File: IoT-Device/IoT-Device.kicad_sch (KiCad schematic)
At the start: 45 parts, among them J1 USB_C_Receptacle_USB2.0_16P, J2 Conn_ARM_JTAG_SWD_10, SW1 B1, SW2 B2, SW3 BOOT_MODE, SW4 RESET, U1 STM32U585VITx, U2 ESP32-C3-WROOM-02, U3 BD33GA5WEFJ

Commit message: add schematics, update metro shield
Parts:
- J1: value USB_C_Receptacle_USB2.0_16P -> USB-C
- J2: value Conn_ARM_JTAG_SWD_10 -> SWD
- U1: value STM32U585VITx -> STM32U585VI
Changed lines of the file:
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@@
 		(dnp no)
 		(property "Reference" "U1"
-			(at 196.088 144.526 0)
-			(effects
-				(font
-					(size 1.27 1.27)
-				)
-			)
-		)
-		(property "Value" "STM32U585VITx"
-			(at 198.628 145.542 0)
+			(at 196.088 154.178 0)
+			(effects
+				(font
+					(size 1.27 1.27)
+				)
+			)
+		)
+		(property "Value" "STM32U585VI"
+			(at 196.088 145.288 0)
 			(effects
 				(font
@@
 			)
 		)
-		(property "Value" "Conn_ARM_JTAG_SWD_10"
+		(property "Value" "SWD"
 			(at 247.65 144.7799 0)
 			(effects
@@
 			)
 		)
-		(property "Value" "USB_C_Receptacle_USB2.0_16P"
+		(property "Value" "USB-C"
 			(at 34.29 24.13 0)
 			(effects

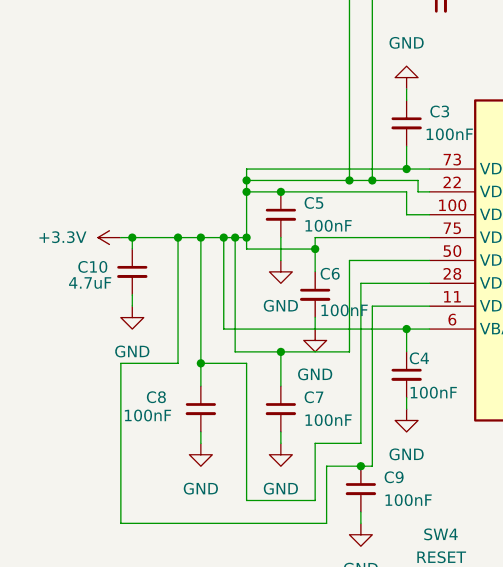
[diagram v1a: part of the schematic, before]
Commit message: update IoT-device schematic, update pcb to free space around more pins
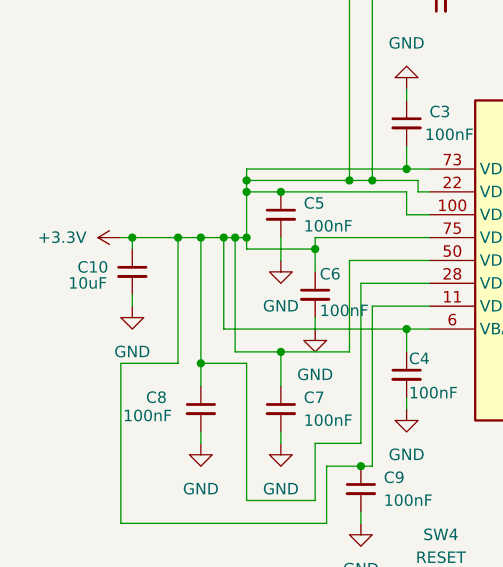
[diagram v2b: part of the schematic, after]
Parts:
- C10: value 4.7uF -> 10uF
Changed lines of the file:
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@@
 			)
 		)
-		(property "Value" "4.7uF"
+		(property "Value" "10uF"
 			(at 17.018 139.7 0)
 			(effects

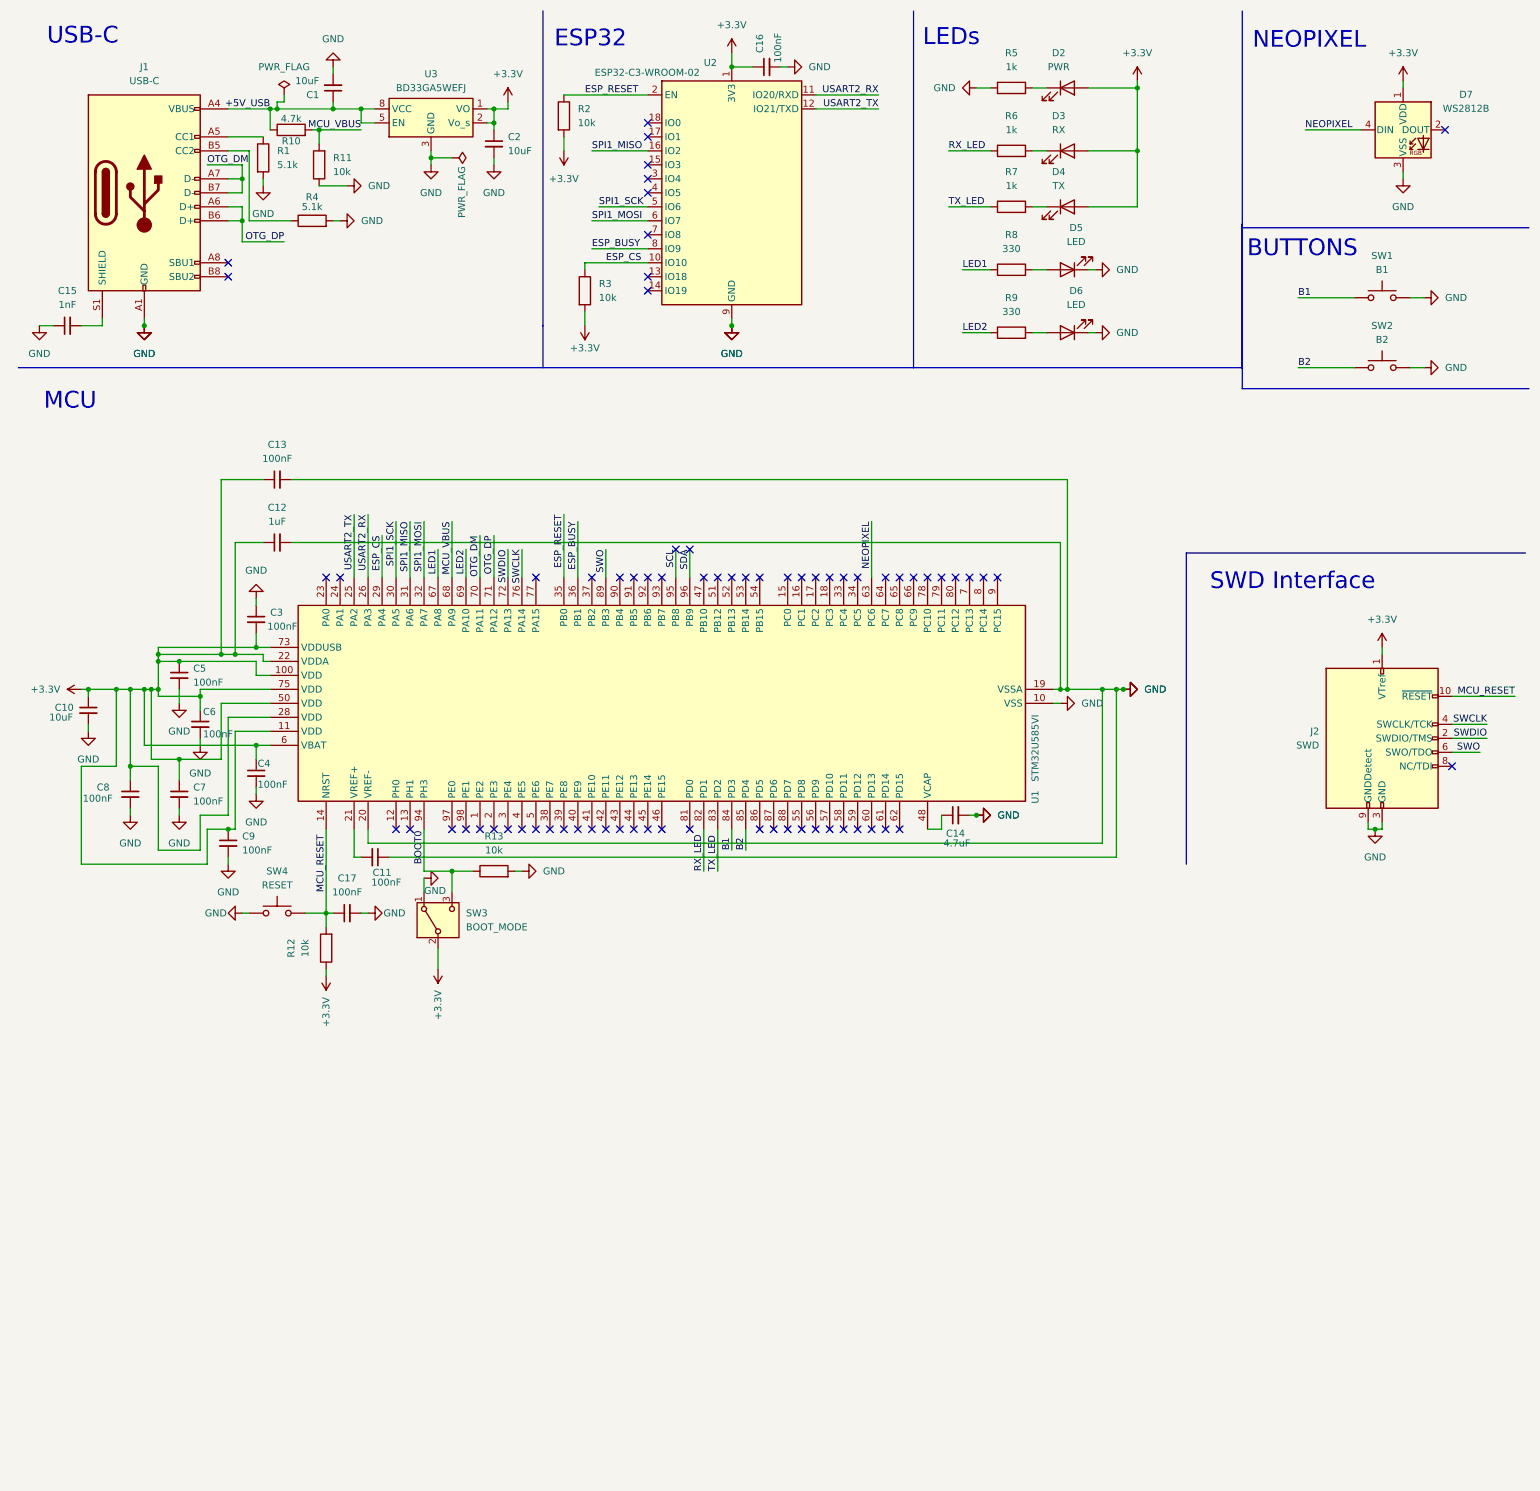
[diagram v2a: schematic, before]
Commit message: add battery power to design
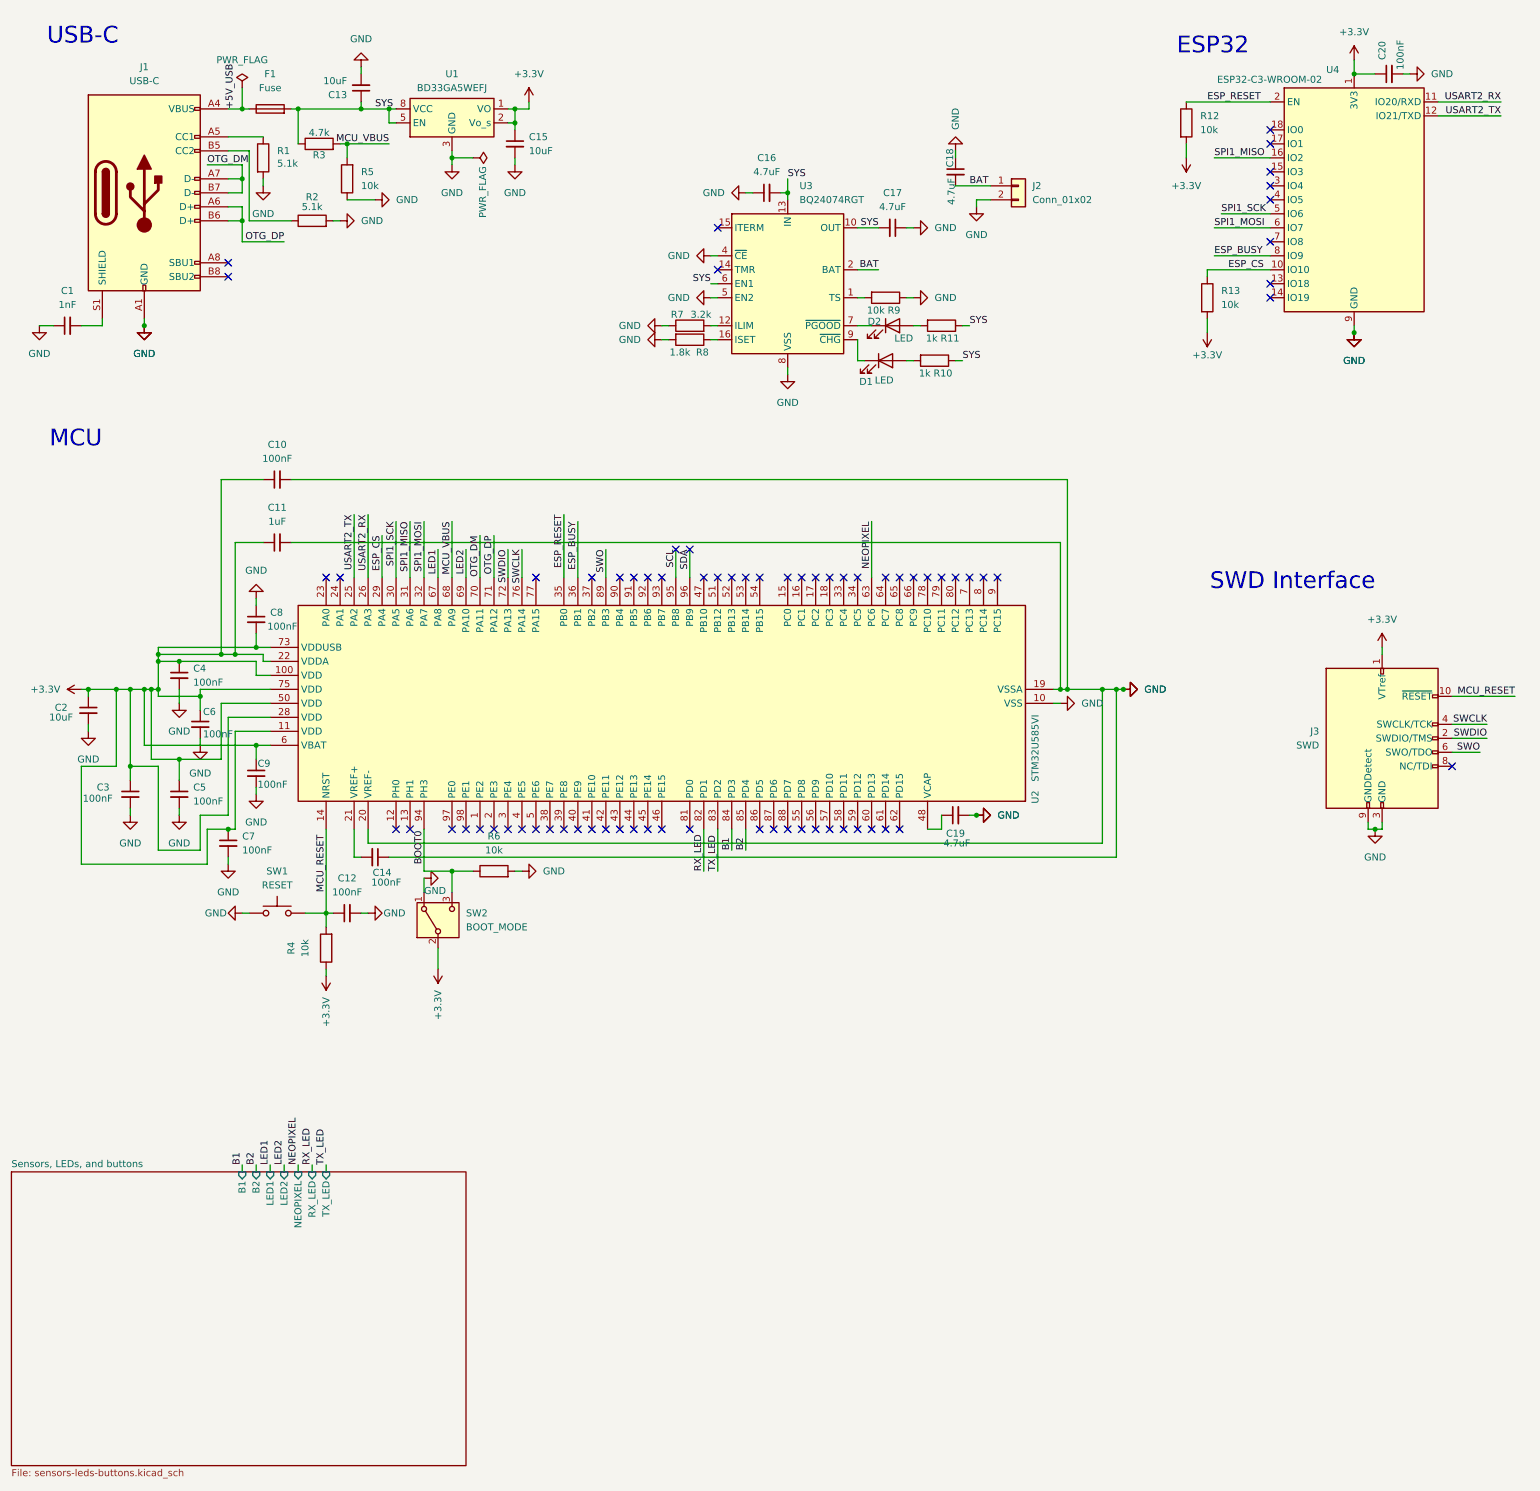
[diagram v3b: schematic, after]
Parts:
- removed D3: RX, LED_SMD:LED_0603_1608Metric, symbol Device:LED
- removed D4: TX, LED_SMD:LED_0603_1608Metric, symbol Device:LED
- removed D5, D6: LED, LED_SMD:LED_0603_1608Metric, symbol Device:LED
- removed D7: WS2812B, LED_SMD:LED_WS2812B_PLCC4_5.0x5.0mm_P3.2mm, symbol LED:WS2812B
- removed R5, R6: 1k, Resistor_SMD:R_0603_1608Metric, symbol Device:R
- removed SW1: B1, Button_Switch_SMD:SW_SPST_PTS647_Sx50, symbol Switch:SW_Push
- removed SW2: B2, Button_Switch_SMD:SW_SPST_PTS647_Sx50, symbol Switch:SW_Push
- added C16, C17, C18: 4.7uF, Capacitor_SMD:C_0603_1608Metric, symbol Device:C_Small
- added D1: LED, LED_SMD:LED_0603_1608Metric, symbol Device:LED
- added F1: Fuse, Fuse:Fuse_0603_1608Metric, symbol Device:Fuse
- added J2: Conn_01x02, Connector_JST:JST_PH_B2B-PH-K_1x02_P2.00mm_Vertical, symbol Connector_Generic:Conn_01x02
- added R10, R11: 1k, Resistor_SMD:R_0603_1608Metric, symbol Device:R
- added U3: BQ24074RGT, Package_DFN_QFN:VQFN-16-1EP_3x3mm_P0.5mm_EP1.6x1.6mm, symbol Battery_Management:BQ24074RGT
- D2: value PWR -> LED
- R7: value 1k -> 3.2k
- R8: value 330 -> 1.8k
- R9: value 330 -> 10k
- renumbered C15 to C1, C13 to C10, C12 to C11, C17 to C12, C1 to C13, C11 to C14, C2 to C15, C14 to C19, C10 to C2, C16 to C20, C8 to C3, C5 to C4, C7 to C5, C9 to C7, C3 to C8, C4 to C9, J2 to J3, R2 to R12, R3 to R13, R4 to R2, R10 to R3, R12 to R4, R11 to R5, R13 to R6, SW4 to SW1, SW3 to SW2, U3 to U1, U1 to U2, U2 to U4
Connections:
- net +3.3V: no longer D2.2 (A)
- net +5V_USB: now also F1.1; no longer C13.1, R3.1, U1.5 (EN), U1.8 (VCC)
- net GND: now also R7.1, R8.2, R9.1, C16.1, C17.1, C18.1, J2.2 (Pin_2), U3.17 (VSS), U3.4 (~{CE}), U3.5 (EN2), U3.8 (VSS)
- net LED1: no longer R8.1
- net LED2: no longer R9.1
- net TX_LED: no longer R7.1
- net at R9.2: now also U3.1 (TS)
- net at D2.1 (K): now also U3.7 (~{PGOOD})
- net at R7.2: now also U3.12 (ILIM)
- new net: D2.2 (A), R11.2
- new net: R8.1, U3.16 (ISET)
- new net: D1.1 (K), U3.9 (~{CHG})
- new net: D1.2 (A), R10.2
- new net BAT: C18.2, J2.1 (Pin_1), U3.2 (BAT), U3.3 (BAT)
- new net SYS: C13.1, C16.2, C17.2, F1.2, R10.1, R11.1, R3.1, U1.5 (EN), U1.8 (VCC), U3.10 (OUT), U3.11 (OUT), U3.13 (IN), U3.6 (EN1)
- no-connect marks 72 -> 73
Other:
- added sheet Sensors, LEDs, and buttons (sensors-leds-buttons.kicad_sch)
- note removed: "BUTTONS"
- note removed: "LEDs"
- note removed: "NEOPIXEL"
- moved on the sheet: C13, C15, C20, R12, R13, R3, R5, U1, U4

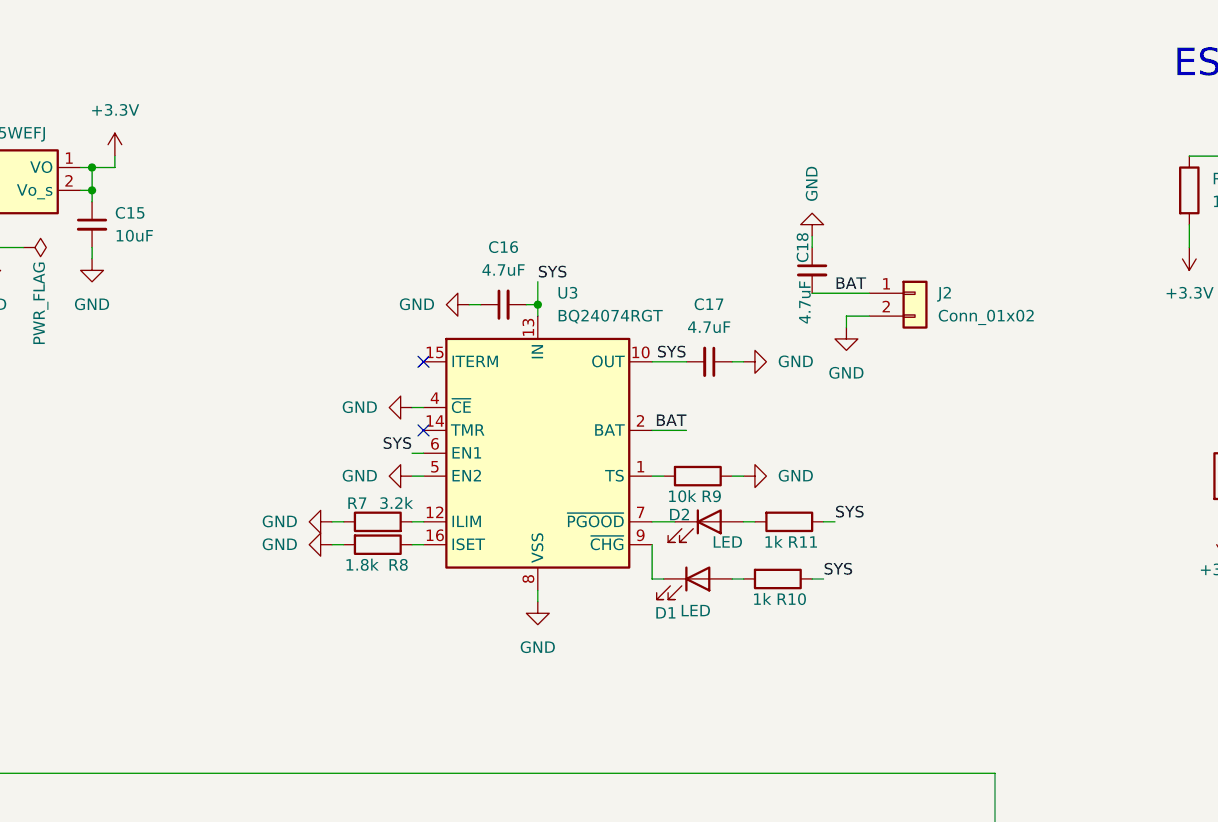
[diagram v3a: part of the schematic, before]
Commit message: add title to battery system section
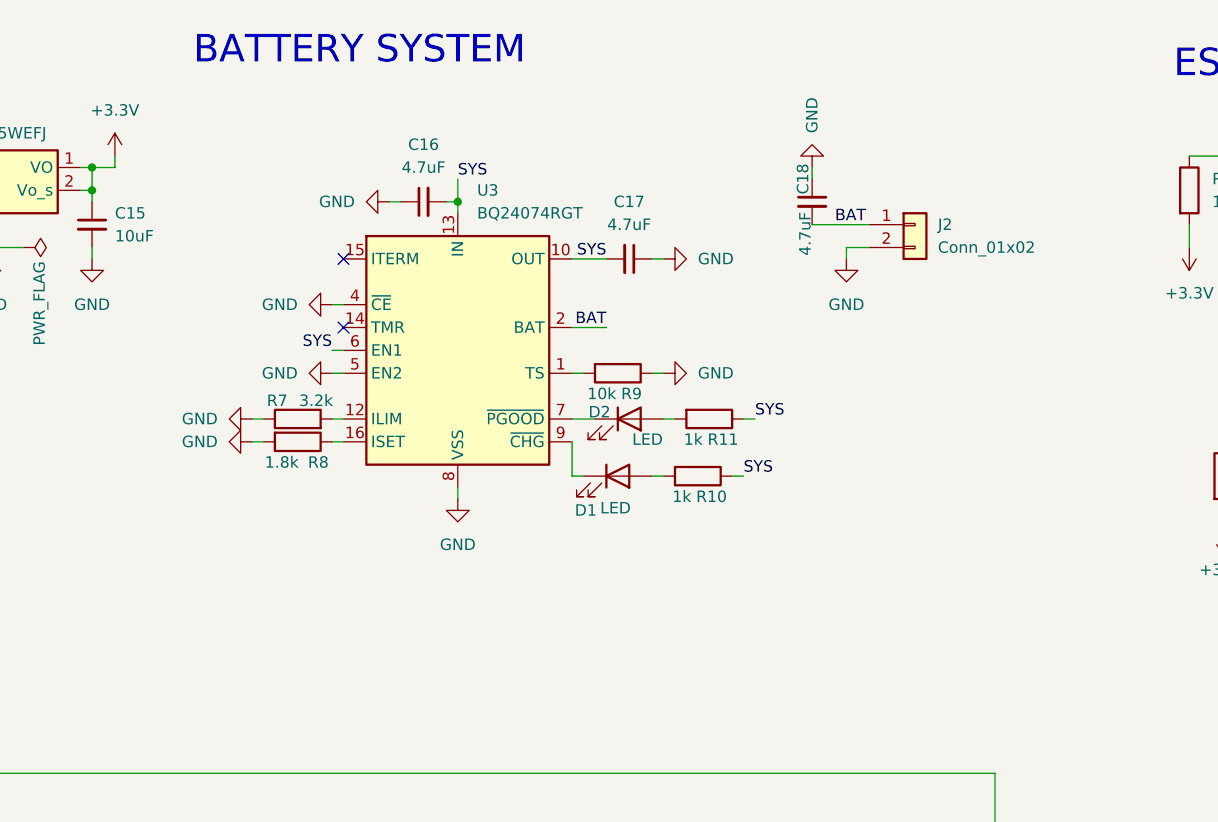
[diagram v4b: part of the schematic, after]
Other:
- note added: "BATTERY SYSTEM"
- moved on the sheet: C16, C17, C18, D1, D2, J2, R10, R11, R7, R8, R9, U3

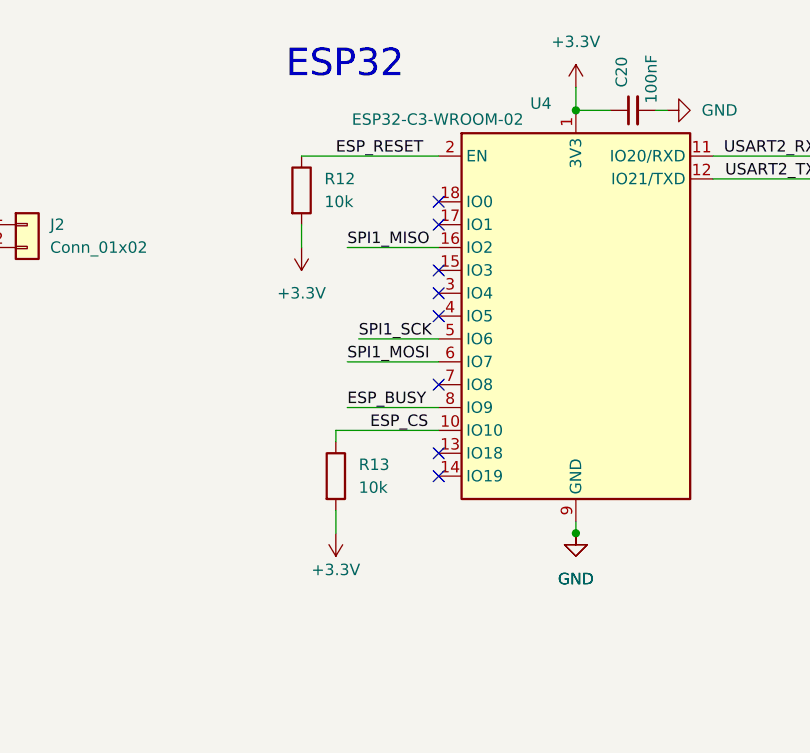
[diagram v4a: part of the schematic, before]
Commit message: fix ESP32 (GPIO2 & GPIO9) issue on schematic
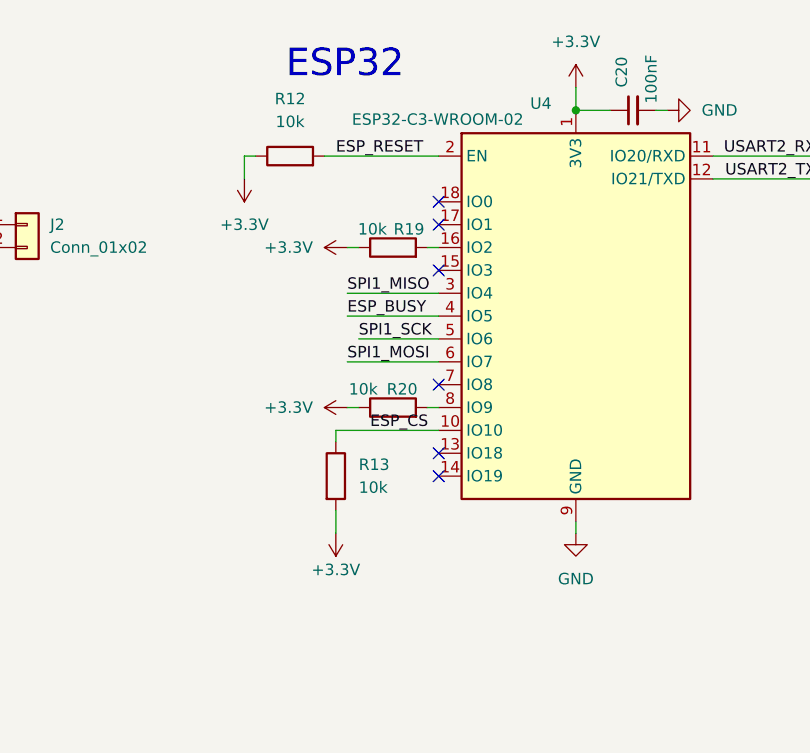
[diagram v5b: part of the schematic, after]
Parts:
- added R19, R20: 10k, Resistor_SMD:R_0603_1608Metric, symbol Device:R
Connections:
- net +3.3V: now also R12.1, R19.1, R20.1; no longer R12.2
- net ESP_BUSY: now also U4.4 (IO5); no longer U4.8 (IO9)
- net ESP_RESET: now also R12.2; no longer R12.1
- net SPI1_MISO: now also U4.3 (IO4); no longer U4.16 (IO2)
- new net: R19.2, U4.16 (IO2)
- new net: R20.2, U4.8 (IO9)
- no-connect marks 73 -> 71
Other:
- moved on the sheet: R12
